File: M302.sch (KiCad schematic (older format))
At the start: 25 parts, among them J1 I2C-SHT3x, J2 I2C-ThmCp, J3 I2C-3, J4 I2C-4, J5 I2C-D400, J6 W5500, J7 IM920, J8 PWR+5V, J9 ANALOG-IN, P1 Power, P2 Analog, P3 Digital, P4 Digital, P5 CONN_01X01, P6 CONN_01X01, P7 CONN_01X01, P8 CONN_01X01, SW1 CPU, SW2 D400, SW3 IM920, U1 SFE-BOB-12009

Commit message: M302改 v1.10 PCB作業途中
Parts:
- R1, R2, R3: footprint Resistor_THT:R_Axial_DIN0207_L6.3mm_D2.5mm_P10.16mm_Horizontal -> Resistor_THT:R_Axial_DIN0207_L6.3mm_D2.5mm_P7.62mm_Horizontal
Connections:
- net A4(SDA): no longer P2.5 (Pin_5)
- net A5(SCL): no longer P2.6 (Pin_6)
- no-connect marks 17 -> 19
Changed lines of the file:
@@
 Text Label 5200 6900 0    60   ~ 0
 A3
-Text Label 5850 4900 0    60   ~ 0
-A4(SDA)
-Text Label 5850 5000 0    60   ~ 0
-A5(SCL)
 Text Label 7500 5000 0    60   ~ 0
 0(Rx)
@@
 F 0 "R1" H 4968 3496 50  0000 L CNN
 F 1 "10k" H 4968 3405 50  0000 L CNN
-F 2 "Resistor_THT:R_Axial_DIN0207_L6.3mm_D2.5mm_P10.16mm_Horizontal" V 4940 3440 50  0001 C CNN
+F 2 "Resistor_THT:R_Axial_DIN0207_L6.3mm_D2.5mm_P7.62mm_Horizontal" V 4940 3440 50  0001 C CNN
 F 3 "~" H 4900 3450 50  0001 C CNN
 	1    4900 3450
@@
 Wire Wire Line
 	7150 3300 8350 3300
-Connection ~ 5400 4900
-Wire Wire Line
-	5400 4900 6350 4900
 Wire Wire Line
 	5300 5000 5300 2150
@@
 Wire Wire Line
 	7150 3200 8250 3200
-Connection ~ 5300 5000
-Wire Wire Line
-	5300 5000 6350 5000
 Wire Wire Line
 	5900 3500 5900 4300
@@
 F 0 "R2" H 5218 4496 50  0000 L CNN
 F 1 "10k" H 5218 4405 50  0000 L CNN
-F 2 "Resistor_THT:R_Axial_DIN0207_L6.3mm_D2.5mm_P10.16mm_Horizontal" V 5190 4440 50  0001 C CNN
+F 2 "Resistor_THT:R_Axial_DIN0207_L6.3mm_D2.5mm_P7.62mm_Horizontal" V 5190 4440 50  0001 C CNN
 F 3 "~" H 5150 4450 50  0001 C CNN
 	1    5150 4450
@@
 $EndComp
 $Comp
-L power:+5V #PWR?
+L power:+5V #PWR0110
 U 1 1 6001A3E5
 P 5150 4150
-F 0 "#PWR?" H 5150 4000 50  0001 C CNN
+F 0 "#PWR0110" H 5150 4000 50  0001 C CNN
 F 1 "+5V" H 5165 4323 50  0000 C CNN
 F 2 "" H 5150 4150 50  0001 C CNN
@@
 F 0 "R3" H 8518 4246 50  0000 L CNN
 F 1 "10k" H 8518 4155 50  0000 L CNN
-F 2 "Resistor_THT:R_Axial_DIN0207_L6.3mm_D2.5mm_P10.16mm_Horizontal" V 8490 4190 50  0001 C CNN
+F 2 "Resistor_THT:R_Axial_DIN0207_L6.3mm_D2.5mm_P7.62mm_Horizontal" V 8490 4190 50  0001 C CNN
 F 3 "~" H 8450 4200 50  0001 C CNN
 	1    8450 4200
@@
 	6000 6850 5600 6850
 $Comp
-L power:GND #PWR?
+L power:GND #PWR0114
 U 1 1 600ED43B
 P 5700 7100
-F 0 "#PWR?" H 5700 6850 50  0001 C CNN
+F 0 "#PWR0114" H 5700 6850 50  0001 C CNN
 F 1 "GND" H 5700 6950 50  0000 C CNN
 F 2 "" H 5700 7100 50  0000 C CNN
@@
 	1350 3100 1350 4600
 $Comp
-L power:+5V #PWR?
+L power:+5V #PWR0115
 U 1 1 6010C04E
 P 4900 3100
-F 0 "#PWR?" H 4900 2950 50  0001 C CNN
+F 0 "#PWR0115" H 4900 2950 50  0001 C CNN
 F 1 "+5V" H 4915 3273 50  0000 C CNN
 F 2 "" H 4900 3100 50  0001 C CNN
@@
 	1    0    0    -1
 $EndComp
+NoConn ~ 6350 4900
+NoConn ~ 6350 5000
 $EndSCHEMATC

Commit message: sche: board: docs:
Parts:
- added C2: 0.01μF, Capacitor_THT:C_Disc_D3.0mm_W2.0mm_P2.50mm, symbol Device:C_Small
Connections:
- net +5V: now also C2.1
- net GND: now also C2.2
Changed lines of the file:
@@
 Sheet 1 1
 Title "M302 Measurement Equipment Type Light"
-Date "2021-01-15"
+Date "2021-02-24"
 Rev "1.10"
 Comp "HOLLY&Co.,Ltd."
 Comment1 "Use W5500 I/F for LAN networking"
 Comment2 "Use IM920 I/F for Radio connection"
-Comment3 ""
+Comment3 "Analog Input 4ch available"
 Comment4 ""
 $EndDescr
@@
 $EndComp
 Wire Wire Line
-	1900 1700 2600 1700
+	1900 1700 2150 1700
 Wire Wire Line
 	3550 1700 3550 1550
@@
 	2600 1950 2600 2000
 Wire Wire Line
-	2600 2000 1900 2000
+	2600 2000 2150 2000
 Connection ~ 1900 2000
 Wire Wire Line
@@
 NoConn ~ 6350 4900
 NoConn ~ 6350 5000
+$Comp
+L Device:C_Small C2
+U 1 1 6036F19A
+P 2150 1850
+F 0 "C2" H 2242 1896 50  0000 L CNN
+F 1 "0.01μF" H 2242 1805 50  0000 L CNN
+F 2 "Capacitor_THT:C_Disc_D3.0mm_W2.0mm_P2.50mm" H 2150 1850 50  0001 C CNN
+F 3 "~" H 2150 1850 50  0001 C CNN
+	1    2150 1850
+	1    0    0    -1
+$EndComp
+Wire Wire Line
+	2150 1750 2150 1700
+Connection ~ 2150 1700
+Wire Wire Line
+	2150 1700 2600 1700
+Wire Wire Line
+	2150 1950 2150 2000
+Connection ~ 2150 2000
+Wire Wire Line
+	2150 2000 1900 2000
 $EndSCHEMATC

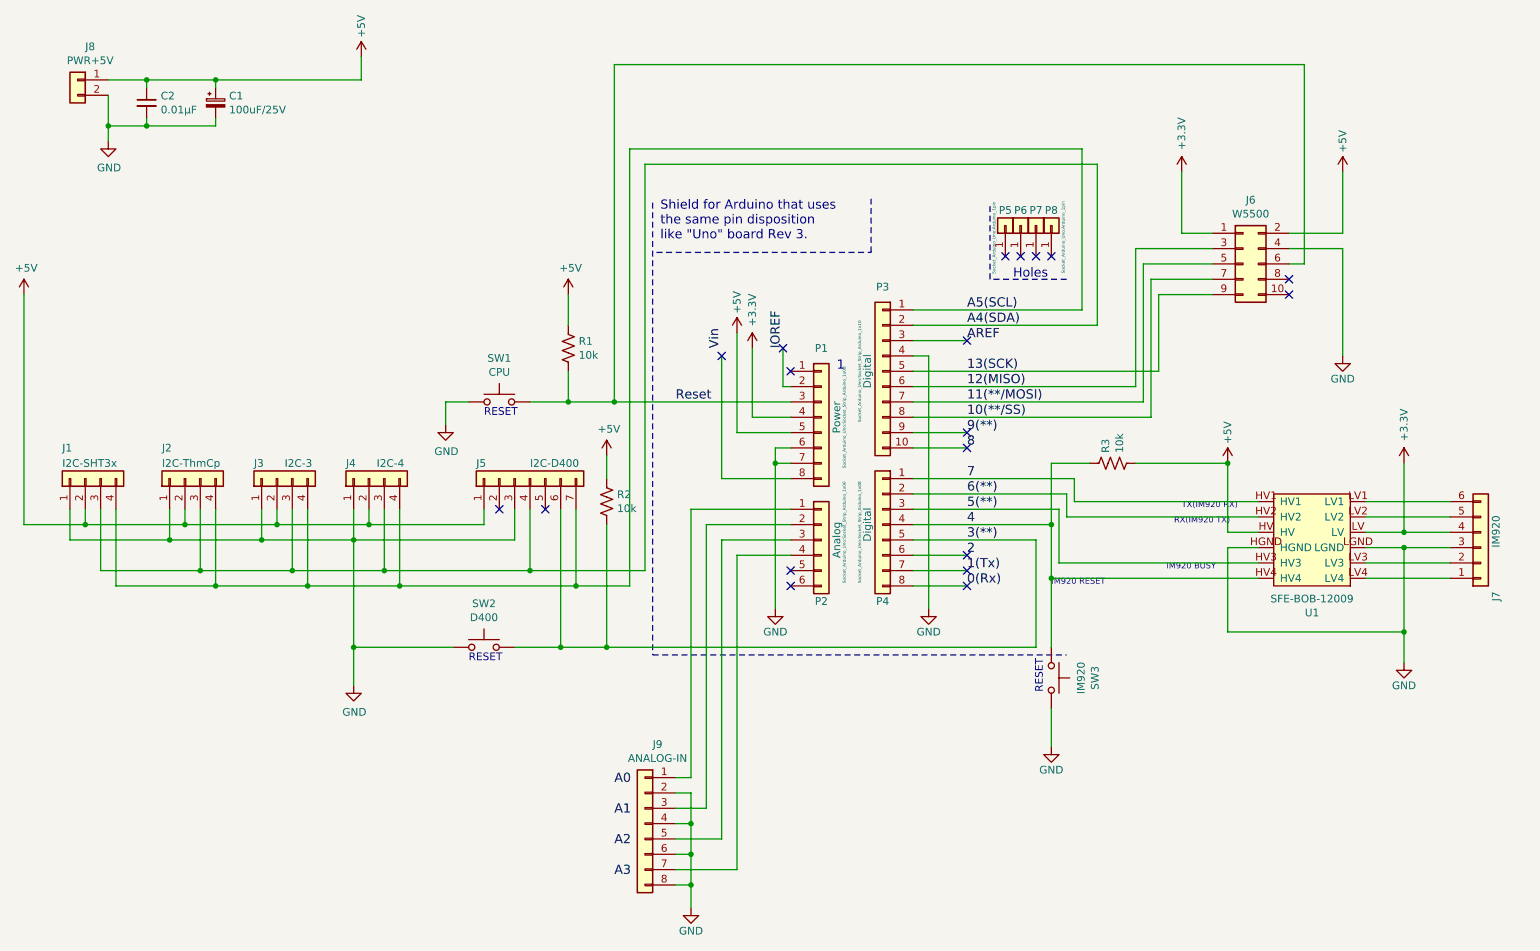
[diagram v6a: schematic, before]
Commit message: rel: 1.11 コンデンサ3Dモデル変更
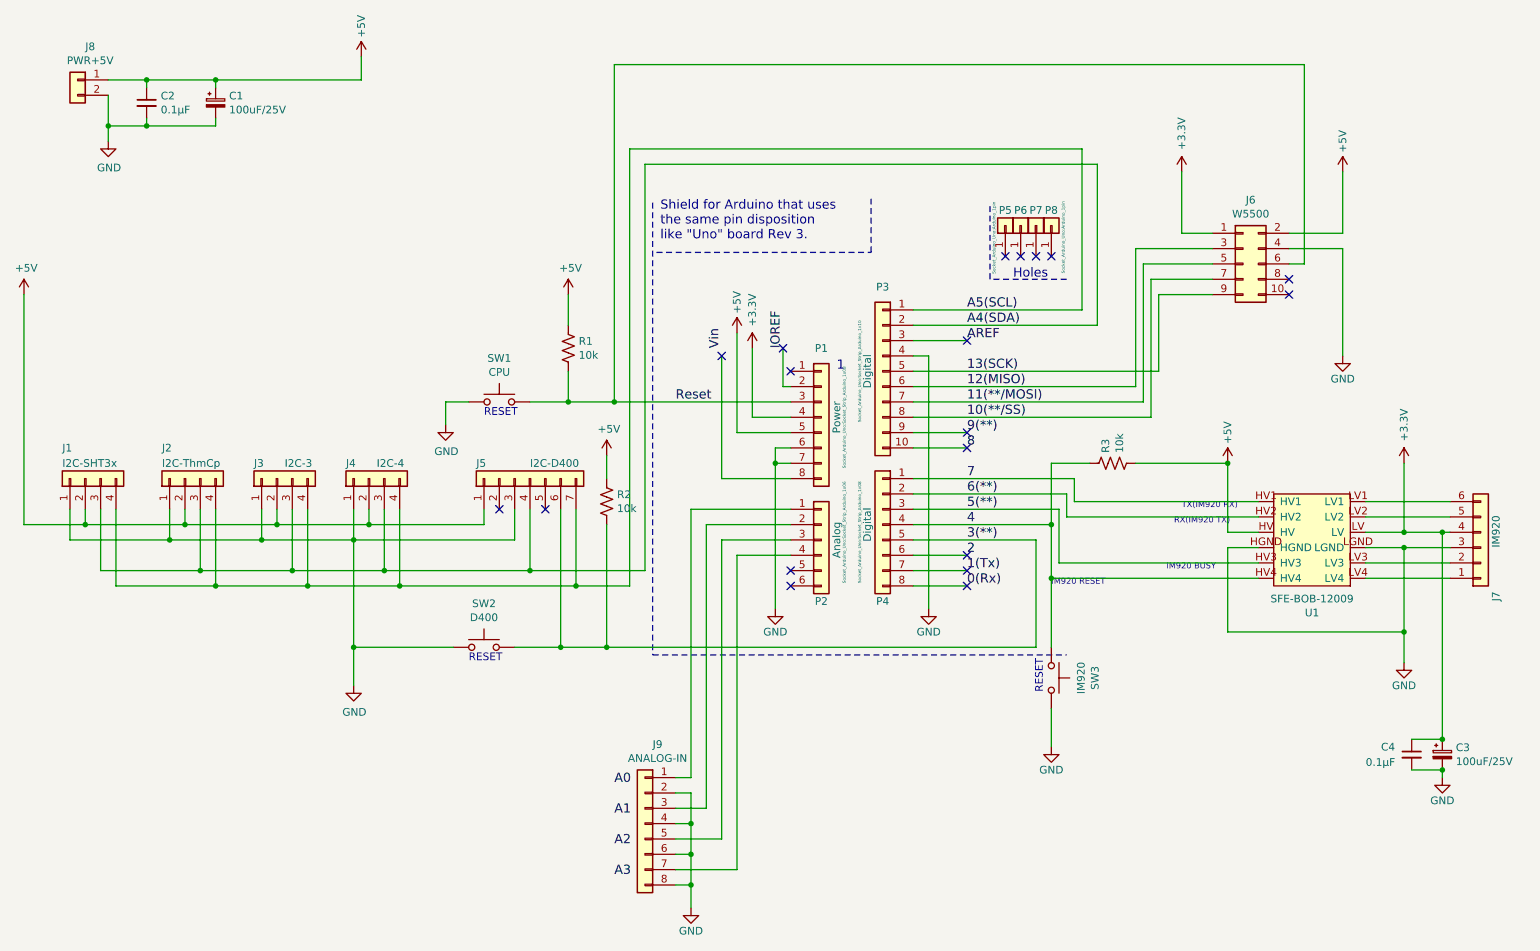
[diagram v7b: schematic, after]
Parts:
- added C3: 100uF/25V, Capacitor_THT:CP_Radial_D5.0mm_P2.00mm, symbol Device:CP_Small
- added C4: 0.1μF, Capacitor_THT:C_Disc_D3.0mm_W2.0mm_P2.50mm, symbol Device:C_Small
- C2: value 0.01μF -> 0.1μF
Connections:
- net +3V3: now also C3.1, C4.1
- net GND: now also C3.2, C4.2
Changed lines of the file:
@@
 	10100 4850 10650 4850
 Wire Wire Line
-	10350 4650 10650 4650
+	10350 4650 10600 4650
 Wire Wire Line
 	10350 4200 10350 4650
@@
 P 2150 1850
 F 0 "C2" H 2242 1896 50  0000 L CNN
-F 1 "0.01μF" H 2242 1805 50  0000 L CNN
+F 1 "0.1μF" H 2242 1805 50  0000 L CNN
 F 2 "Capacitor_THT:C_Disc_D3.0mm_W2.0mm_P2.50mm" H 2150 1850 50  0001 C CNN
 F 3 "~" H 2150 1850 50  0001 C CNN
@@
 Wire Wire Line
 	2150 2000 1900 2000
+$Comp
+L Device:CP_Small C3
+U 1 1 60391113
+P 10600 6100
+F 0 "C3" H 10688 6146 50  0000 L CNN
+F 1 "100uF/25V" H 10688 6055 50  0000 L CNN
+F 2 "Capacitor_THT:CP_Radial_D5.0mm_P2.00mm" H 10600 6100 50  0001 C CNN
+F 3 "https://akizukidenshi.com/download/ds/rubycon/PK_series.pdf" H 10600 6100 50  0001 C CNN
+	1    10600 6100
+	1    0    0    -1
+$EndComp
+$Comp
+L Device:C_Small C4
+U 1 1 60391E4E
+P 10400 6100
+F 0 "C4" H 10200 6150 50  0000 L CNN
+F 1 "0.1μF" H 10100 6050 50  0000 L CNN
+F 2 "Capacitor_THT:C_Disc_D3.0mm_W2.0mm_P2.50mm" H 10400 6100 50  0001 C CNN
+F 3 "~" H 10400 6100 50  0001 C CNN
+	1    10400 6100
+	1    0    0    -1
+$EndComp
+Wire Wire Line
+	10600 4650 10600 6000
+Connection ~ 10600 4650
+Wire Wire Line
+	10600 4650 10650 4650
+Wire Wire Line
+	10400 6000 10600 6000
+Connection ~ 10600 6000
+Wire Wire Line
+	10400 6200 10600 6200
+$Comp
+L power:GND #PWR0116
+U 1 1 603AD11B
+P 10600 6250
+F 0 "#PWR0116" H 10600 6000 50  0001 C CNN
+F 1 "GND" H 10600 6100 50  0000 C CNN
+F 2 "" H 10600 6250 50  0000 C CNN
+F 3 "" H 10600 6250 50  0000 C CNN
+	1    10600 6250
+	1    0    0    -1
+$EndComp
+Wire Wire Line
+	10600 6250 10600 6200
+Connection ~ 10600 6200
 $EndSCHEMATC
